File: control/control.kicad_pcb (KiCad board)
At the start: 4 copper layers, 45.7 x 39.4 mm, 90 parts, among them M1 LMR62014, M2 LM46001, M3 STM32F4XX, M4 TPS736XX, M5 SN65HVD23X, P1 ENCODER, P2 VOLTAGE, P3 CONTROL, P4 POWER, P5 SENSOR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

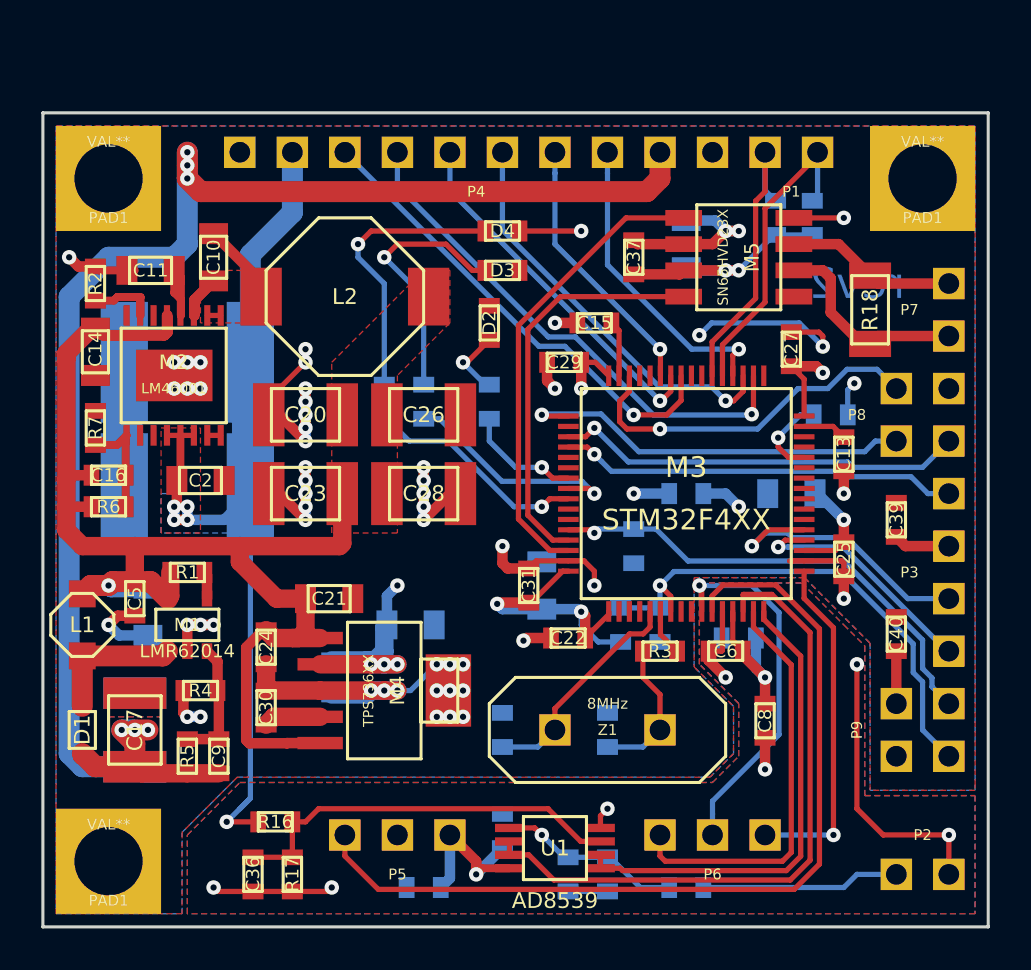
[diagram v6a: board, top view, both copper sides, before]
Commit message: Accumulated changes, large track width, encoder/hall interface, etc.
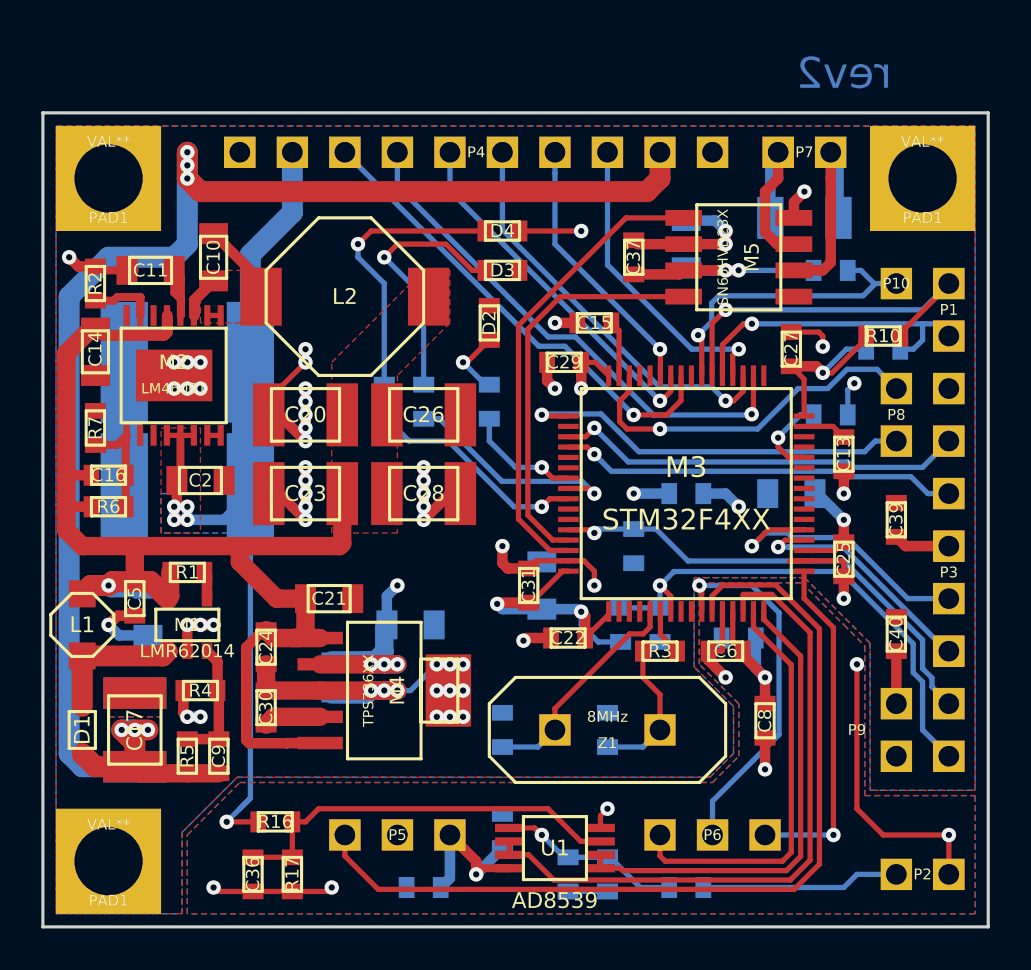
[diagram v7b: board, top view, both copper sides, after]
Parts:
- added P10: HALL_C, foot:PLS1, F.Cu at (138.4, 68.6)
- added R12: 10K, foot:SM0603, B.Cu at (135.3, 67.9)
- C17, C19: value 4.7uF -> 10uF
- C18, C8: value 100nF -> 10nF
- P1: value ENCODER -> ENCODER_AB
- P4: value POWER -> POWER/FETS
- P5: value SENSOR -> SENSOR_A
- P6: value SENSOR -> SENSOR_B
- P9: value JUMPER -> SUPPLY
- R10: moved to F.Cu
- R18: moved to B.Cu
- moved P1 10.8 mm to (141.0, 69.8), turned to 90 degrees
- moved P7 10.3 mm to (134.0, 62.2), turned to 0 degrees
- moved R10 7.73 mm to (137.8, 71.1), turned to 180 degrees
- moved R9 7.22 mm to (137.8, 71.8), turned to 180 degrees
- moved R18 5.46 mm to (134.0, 65.4), turned to 180 degrees
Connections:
- M3 pad 39: Net-(M3-Pad39) -> EN_C
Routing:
- net EN_C: track 0.00 -> 14.8 mm, vias 0 -> 1
- net GND: track 133.8 -> 125.9 mm, vias 64 -> 63
- net +3.3V: track 73.8 -> 78.6 mm
- net EN_B: track 14.4 -> 18.3 mm, vias 0 -> 1
- net Net-(M5-Pad7): track 8.28 -> 9.10 mm
- net Net-(M5-Pad6): track 10.1 -> 10.6 mm
- net EN_A: vias 0 -> 1

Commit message: Reduced decoupling capacitor bank like ESC, also added two row of pins, small fixes.
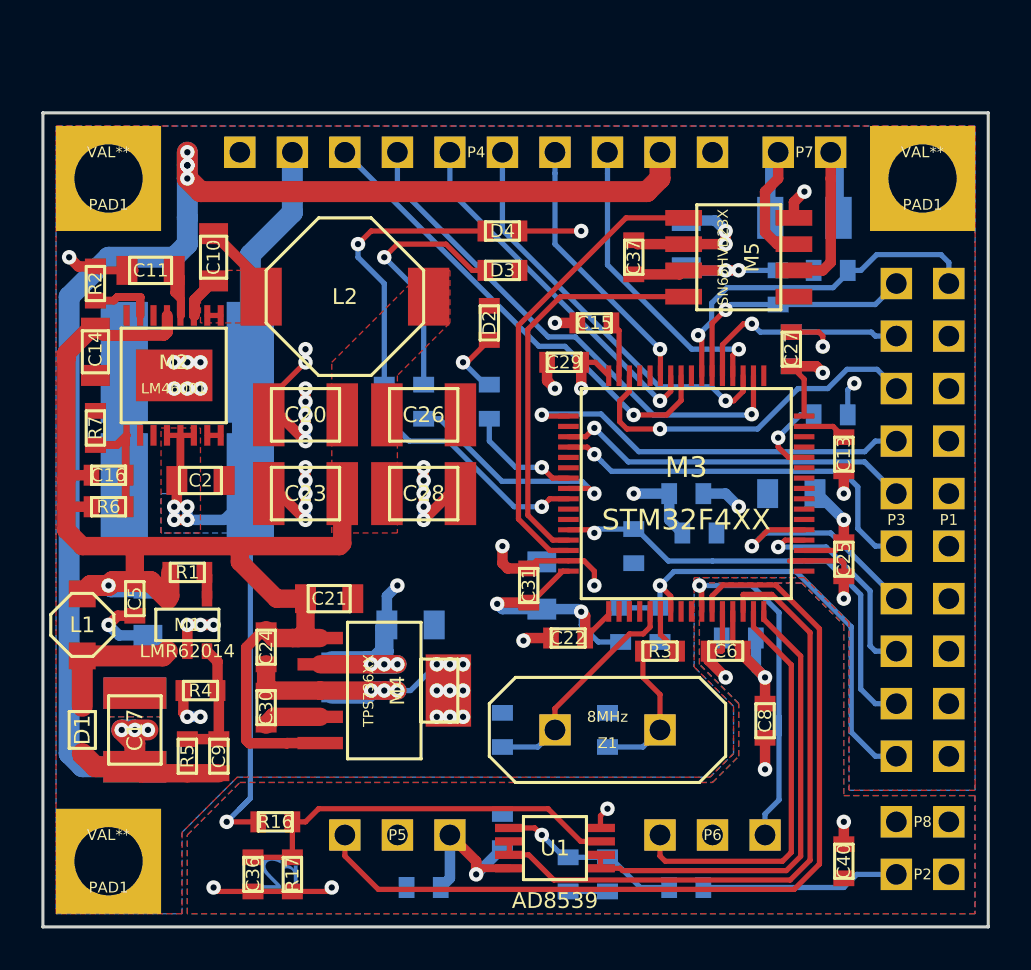
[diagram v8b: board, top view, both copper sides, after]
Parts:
- removed P10: HALL_C, foot:PLS1
- removed P9: SUPPLY, foot:PLS2
- C39, R10: moved to B.Cu
- P1: value ENCODER_AB -> GND/VDD; footprint foot:PLS2 -> foot:PLS10
- P3: value CONTROL -> INTERFACE; footprint foot:PLS8 -> foot:PLS10
- P8: value SWD -> ANALOG
- moved P8 19.7 mm to (139.7, 94.6), turned to 180 degrees
- moved C40 11.3 mm to (135.9, 96.5), turned to 270 degrees
- moved P1 10.2 mm to (141.0, 80.0), turned to 270 degrees
- moved C39 9.55 mm to (128.9, 80.6), turned to 0 degrees
- moved R10 5.60 mm to (132.7, 68.8), turned to 90 degrees
- moved R9 4.44 mm to (133.3, 71.8), turned to 270 degrees
- moved P3 3.59 mm to (138.4, 80.0)
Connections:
- M3 pad 46: Net-(M3-Pad46) -> SWDIO
- M3 pad 49: Net-(M3-Pad49) -> SWDCLK
- P1 pad 1: EN_A -> EN_C
- P1 pad 2: EN_B -> GND
- P3 pad 1: GND -> EN_B
- P3 pad 2: USART_TX -> EN_A
- P3 pad 3: USART_RX -> SWDIO
- P3 pad 4: +3.3V -> SWDCLK
- P3 pad 5: DAC_OUT2 -> USART_TX
- P3 pad 6: DAC_OUT1 -> USART_RX
- P3 pad 7: BOOT -> DAC_OUT2
- P3 pad 8: NRST -> DAC_OUT1
- P6 pad 2: ADC_IN12 -> GND
- P6 pad 3: ADC_IN3 -> ADC_IN12
- P8 pad 1: Net-(M3-Pad46) -> +3.3V
- P8 pad 2: Net-(M3-Pad49) -> GND
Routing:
- net SWDCLK: track 0.00 -> 19.4 mm, vias 0 -> 1
- net Net-(M3-Pad49): track 19.4 -> 0.00 mm, vias 1 -> 0
- net SWDIO: track 0.00 -> 17.5 mm, vias 0 -> 1
- net Net-(M3-Pad46): track 17.5 -> 0.00 mm, vias 1 -> 0
- net ADC_IN3: track 16.7 -> 0.00 mm, vias 1 -> 0
- net GND: track 125.9 -> 112.1 mm, vias 63 -> 61
- net EN_B: track 18.3 -> 12.2 mm
- net +3.3V: track 78.6 -> 72.8 mm, vias 14 -> 15
- net EN_A: track 15.2 -> 10.7 mm
- net EN_C: track 14.8 -> 17.6 mm
- net USART_TX: track 19.9 -> 17.4 mm
- net DAC_OUT2: track 14.0 -> 11.4 mm
- net NRST: track 24.6 -> 22.8 mm
- net DAC_OUT1: track 11.7 -> 10.7 mm
- net BOOT: track 23.2 -> 23.9 mm
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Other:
- board text added: "r2"
- board text removed: "rev2"
